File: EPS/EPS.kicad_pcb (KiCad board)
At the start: 2 copper layers, 219 parts, among them J1 CAN_BUS, J10 BOOT1, J11 ST_LINK, J12 USART, J9 BOOT0, Q1 Q_NMOS_GSD, Q10 Q_NMOS_GSD, Q11 Q_PMOS_GSD, Q12 Q_NMOS_DGS, Q13 PMOS_IN, Q14 Q_NMOS_GSD, Q15 PMOS_IN, Q16 PMOS_OUT1, Q17 PMOS_OUT2, Q18 NMOS_MCU, Q2 Q_NMOS_GSD, Q3 Q_NMOS_GSD, Q4 Q_NMOS_GSD, Q5 Q_PMOS_GSD, Q6 Q_NMOS_GSD, Q7 Q_NMOS_GSD, Q8 Q_PMOS_GSD, Q9 Q_PMOS_GSD, U1 MCP4728, U2 SN65HVD232, U3 SN65HVD232

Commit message: PCB updated
Added testpoints and updated PCB
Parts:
- removed 5V_1, 5V_2, Batt_V_1, Batt_V_2: Jst_Conn, Connectors_JST:JST_XH_B02B-XH-A_02x2.50mm_Straight
- removed J10: BOOT1, Pin_Headers:Pin_Header_Straight_1x03_Pitch2.54mm
- removed J9: BOOT0, Pin_Headers:Pin_Header_Straight_1x03_Pitch2.54mm
- removed Q18: NMOS_MCU, TO_SOT_Packages_SMD:SOT-23
- removed R5: 168k6, Resistors_SMD:R_0603
- removed R6: 30k1, Resistors_SMD:R_0603
- removed R62, R63, R64: R, Resistors_SMD:R_0603
- removed TPS1: TPS7A7002, Housings_SOIC:SOIC-8_3.9x4.9mm_Pitch1.27mm
- removed Temp_Connector1: JST_conn, Connectors_JST:JST_XH_B02B-XH-A_02x2.50mm_Straight
- added 3V6_1: Jst_Conn, Connectors_JST:JST_XH_B02B-XH-A_02x2.50mm_Straight, F.Cu at (145.5, 103.8)
- added 3V6_2: Jst_Conn, Connectors_JST:JST_XH_B02B-XH-A_02x2.50mm_Straight, F.Cu at (129.8, 103.5)
- added BOOT0: BOOT0, Pin_Headers:Pin_Header_Straight_1x03_Pitch2.54mm, F.Cu at (102.5, 103.8)
- added BOOT1: BOOT1, Pin_Headers:Pin_Header_Straight_1x03_Pitch2.54mm, F.Cu at (102.5, 94.8)
- added BU1: BU33SD5, Housings_SSOP:TSOP-5_1.65x3.05mm_Pitch0.95mm, F.Cu at (163.2, 106.2)
- added D4: LED, LEDs:LED_0603, F.Cu at (102.2, 87.8)
- added R65: 100, Resistors_SMD:R_0603, F.Cu at (106.2, 87.8)
- added RAW1: Jst_Conn, Connectors_JST:JST_XH_B02B-XH-A_02x2.50mm_Straight, F.Cu at (176.0, 91.8)
- added TP1: TEST, Measurement_Points:Measurement_Point_Round-SMD-Pad_Small, F.Cu at (121.9, 31.0)
- added TP10: TEST, Measurement_Points:Measurement_Point_Round-SMD-Pad_Small, F.Cu at (168.9, 31.2)
- added TP11: TEST, Measurement_Points:Measurement_Point_Round-SMD-Pad_Small, F.Cu at (125.0, 32.0)
- added TP12: TEST, Measurement_Points:Measurement_Point_Round-SMD-Pad_Small, F.Cu at (146.6, 32.3)
- added TP13: TEST, Measurement_Points:Measurement_Point_Round-SMD-Pad_Small, F.Cu at (122.9, 47.0)
- added TP14: TEST, Measurement_Points:Measurement_Point_Round-SMD-Pad_Small, F.Cu at (143.5, 46.5)
- added TP15: TEST, Measurement_Points:Measurement_Point_Round-SMD-Pad_Small, F.Cu at (166.9, 51.8)
- added TP16: TEST, Measurement_Points:Measurement_Point_Round-SMD-Pad_Small, F.Cu at (122.4, 53.8)
- added TP17: TEST, Measurement_Points:Measurement_Point_Round-SMD-Pad_Small, F.Cu at (128.0, 55.6)
- added TP18: TEST, Measurement_Points:Measurement_Point_Round-SMD-Pad_Small, F.Cu at (131.1, 58.2)
- added TP19: TEST, Measurement_Points:Measurement_Point_Round-SMD-Pad_Small, F.Cu at (148.1, 63.2)
- added TP2: TEST, Measurement_Points:Measurement_Point_Round-SMD-Pad_Small, F.Cu at (139.4, 31.0)
- added TP20: TEST, Measurement_Points:Measurement_Point_Round-SMD-Pad_Small, F.Cu at (148.1, 61.2)
- added TP21: TEST, Measurement_Points:Measurement_Point_Round-SMD-Pad_Small, F.Cu at (172.5, 55.9)
- added TP22: TEST, Measurement_Points:Measurement_Point_Round-SMD-Pad_Small, F.Cu at (176.0, 46.7)
- added TP23: TEST, Measurement_Points:Measurement_Point_Round-SMD-Pad_Small, F.Cu at (150.1, 55.1)
- added TP24: TEST, Measurement_Points:Measurement_Point_Round-SMD-Pad_Small, F.Cu at (156.7, 52.1)
- added TP25: TEST, Measurement_Points:Measurement_Point_Round-SMD-Pad_Small, F.Cu at (94.5, 72.1)
- added TP26: TEST, Measurement_Points:Measurement_Point_Round-SMD-Pad_Small, F.Cu at (94.5, 75.4)
- added TP27: TEST, Measurement_Points:Measurement_Point_Round-SMD-Pad_Small, F.Cu at (116.6, 22.1)
- added TP3: TEST, Measurement_Points:Measurement_Point_Round-SMD-Pad_Small, F.Cu at (157.5, 30.7)
- added TP4: TEST, Measurement_Points:Measurement_Point_Round-SMD-Pad_Small, F.Cu at (115.8, 28.7)
- added TP5: TEST, Measurement_Points:Measurement_Point_Round-SMD-Pad_Small, F.Cu at (133.6, 31.8)
- added TP6: TEST, Measurement_Points:Measurement_Point_Round-SMD-Pad_Small, F.Cu at (152.4, 31.5)
- added TP7: TEST, Measurement_Points:Measurement_Point_Round-SMD-Pad_Small, F.Cu at (167.1, 45.5)
- added TP8: TEST, Measurement_Points:Measurement_Point_Round-SMD-Pad_Small, F.Cu at (128.5, 44.2)
- added TP9: TEST, Measurement_Points:Measurement_Point_Round-SMD-Pad_Small, F.Cu at (149.9, 44.2)
- ABM3, C1, C10, C11, C12, C13, C14, C15, C16, C4, C5, C6, C7, C8, C9, L1, R3, R4, STM1, U2, U3: moved to B.Cu
- C2: value 0.1u -> 4.7u
- J1: footprint Housings_SOIC:SOIC-8_3.9x4.9mm_Pitch1.27mm -> Pin_Headers:Pin_Header_Straight_1x03_Pitch2.54mm
- Q5, Q8, Q9: value Q_PMOS_GSD -> PMOS_DIGITAL_LOAD?
- R_s4, R_s5, R_s6, R_s7, R_s8, R_s9: footprint Resistors_SMD:R_0603 -> Resistors_SMD:R_0805
- moved J1 221.4 mm to (190.6, 101.0)
- moved R4 218.7 mm to (184.4, 107.0), turned to 90 degrees
- moved R3 218.5 mm to (184.4, 101.2), turned to 90 degrees
- moved C15 201.6 mm to (172.4, 101.4), turned to 270 degrees
- moved C3 199.9 mm to (166.2, 106.0), turned to 270 degrees
- moved U2 196.1 mm to (177.4, 101.0)
- moved C54 195.1 mm to (147.2, 99.0), turned to 270 degrees
- moved C2 193.1 mm to (160.0, 106.0), turned to 270 degrees
- moved C9 193.0 mm to (152.5, 79.0), turned to 270 degrees
- moved U3 189.4 mm to (177.4, 106.8)
- moved C8 185.1 mm to (149.8, 65.5), turned to 90 degrees
- moved C6 183.8 mm to (146.8, 65.5), turned to 90 degrees
- moved C4 173.2 mm to (141.2, 65.5), turned to 90 degrees
- moved C1 172.5 mm to (131.2, 68.5), turned to 180 degrees
- moved STM1 167.1 mm to (144.0, 74.5)
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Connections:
- net /STM32_block/I_BATT2 renamed Net-(STM1-Pad25)
- BQ1 pad 5: GND -> /SW3
- BQ1 pad 6: GND -> /SW3
- BT2 pad 2: GND -> /SW3
- C57 pad 2: GND -> /SW3
- C58 pad 2: GND -> /SW3
- C59 pad 2: GND -> /SW3
- LM335A1 pad 1: /Battery_pack/BATT_TEMP -> /TEMP_BATT
- LM335A1 pad 2: GND -> /SW3
- MAX4 pad 3: /Connectors_diodes/Diode_enable -> /DIODE_EN
- MAX40200_1 pad 3: /Connectors_diodes/Diode_enable -> /DIODE_EN
- MAX5 pad 3: /Connectors_diodes/Diode_enable -> /DIODE_EN
- MAX6 pad 3: /Connectors_diodes/Diode_enable -> /DIODE_EN
- MAX7 pad 3: /Connectors_diodes/Diode_enable -> /DIODE_EN
- MAX8 pad 3: /Connectors_diodes/Diode_enable -> /DIODE_EN
- Q12 pad 2: /Battery_pack/BATT_HEATER -> /HEATER_EN
- Q12 pad 3: GND -> /SW3
- Q16 pad 1: Net-(Q16-Pad1) -> /SW2
- Q17 pad 1: Net-(Q16-Pad1) -> /SW2
- R48 pad 2: /Battery_pack/BATT_CELL2_VOLTAGE -> /BATT_V2
- R49 pad 2: /Battery_pack/BATT_CELL1_VOLTAGE -> /BATT_V1
- R50 pad 2: /Battery_pack/BATT_CELL2_VOLTAGE -> /BATT_V2
- R51 pad 2: /Battery_pack/BATT_CELL1_VOLTAGE -> /BATT_V1
- R56 pad 2: /Battery_pack/BATT_TEMP -> /TEMP_BATT
- R57 pad 1: /Battery_pack/BATT_HEATER -> /HEATER_EN
- R61 pad 1: /Battery_pack/BATT+ -> /SW2
- R61 pad 2: Net-(Q16-Pad1) -> /Battery_pack/BATT+
- RBF_control_pins1 pad 5: GND -> /SW3
- STM1 pad 16: Net-(STM1-Pad16) -> /TEMP_BATT
- STM1 pad 26: /STM32_block/TEMP_BATT1 -> /BATT_V1
- STM1 pad 27: /STM32_block/TEMP_BATT2 -> /BATT_V2
- STM1 pad 36: /3V6_BUS_SW2 -> /3V6_BUS_SW1
- STM1 pad 37: /STM32_block/BATT2_BUS_SW -> /INPUT_PWR_SW
- STM1 pad 39: /MAIN_PWR_SW -> Net-(STM1-Pad39)
- STM1 pad 51: Net-(STM1-Pad51) -> /DIODE_EN
- STM1 pad 52: Net-(STM1-Pad52) -> /HEATER_EN
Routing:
- net +3V3: track 8.05 -> 80.3 mm, vias 0 -> 4
- net GND: track 114.7 -> 160.6 mm, vias 14 -> 23
- net Net-(BT1-Pad2): track 0.00 -> 45.6 mm
- net /DIODE_EN: track 0.00 -> 40.2 mm, vias 0 -> 6
- net /Connectors_diodes/Diode_enable: track 38.0 -> 0.00 mm, vias 6 -> 0
- net /Input/Current_Limiters/DAC3: track 35.4 -> 0.00 mm, vias 2 -> 0
- net /SW3: track 0.00 -> 33.4 mm
- net /CAN_H: track 0.00 -> 31.3 mm
- net /SW2: track 0.00 -> 29.2 mm
- net /SW1: track 3.25 -> 32.0 mm, vias 0 -> 1
- net /Z_PV: track 21.9 -> 50.5 mm, vias 1 -> 2
- net Net-(OPAMP3-Pad3): track 33.7 -> 7.10 mm
- net /CAN_L: track 0.00 -> 25.7 mm, vias 0 -> 2
- net /X_PV: track 29.0 -> 45.7 mm
- net Net-(OPAMP1-Pad3): track 24.0 -> 7.73 mm
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- added copper zone on In1.Cu, net +3V3
- added copper zone on B.Cu, net GND
- added copper zone on In2.Cu, net GND
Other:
- board outline added: 100 x 100 mm
- copper layers 2 -> 4
- board text added: "+3V3"
- board text added: "CAN_H"
- board text added: "CAN_L"
- board text added: "GND"
- board text added: "NRST"
- board text added: "SWCLK"
- board text added: "SWDIO"
- board text added: "USART_RX"
- board text added: "USART_TX"

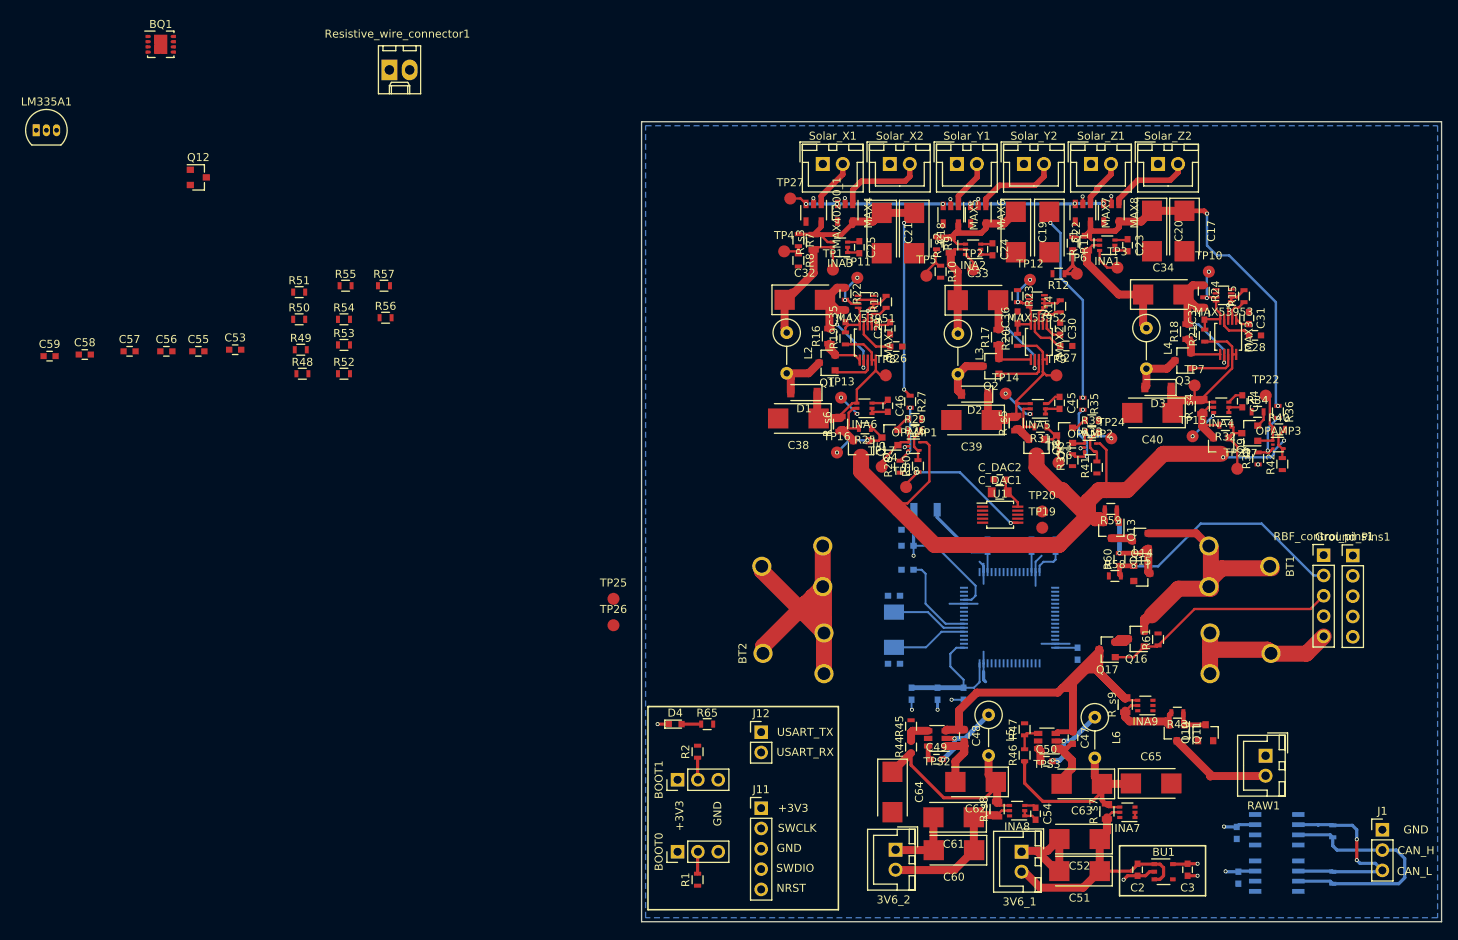
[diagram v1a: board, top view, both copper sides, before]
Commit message: Updated PCB
PCB requires mcu to be routed.
Changed to thermistor connector on pcb
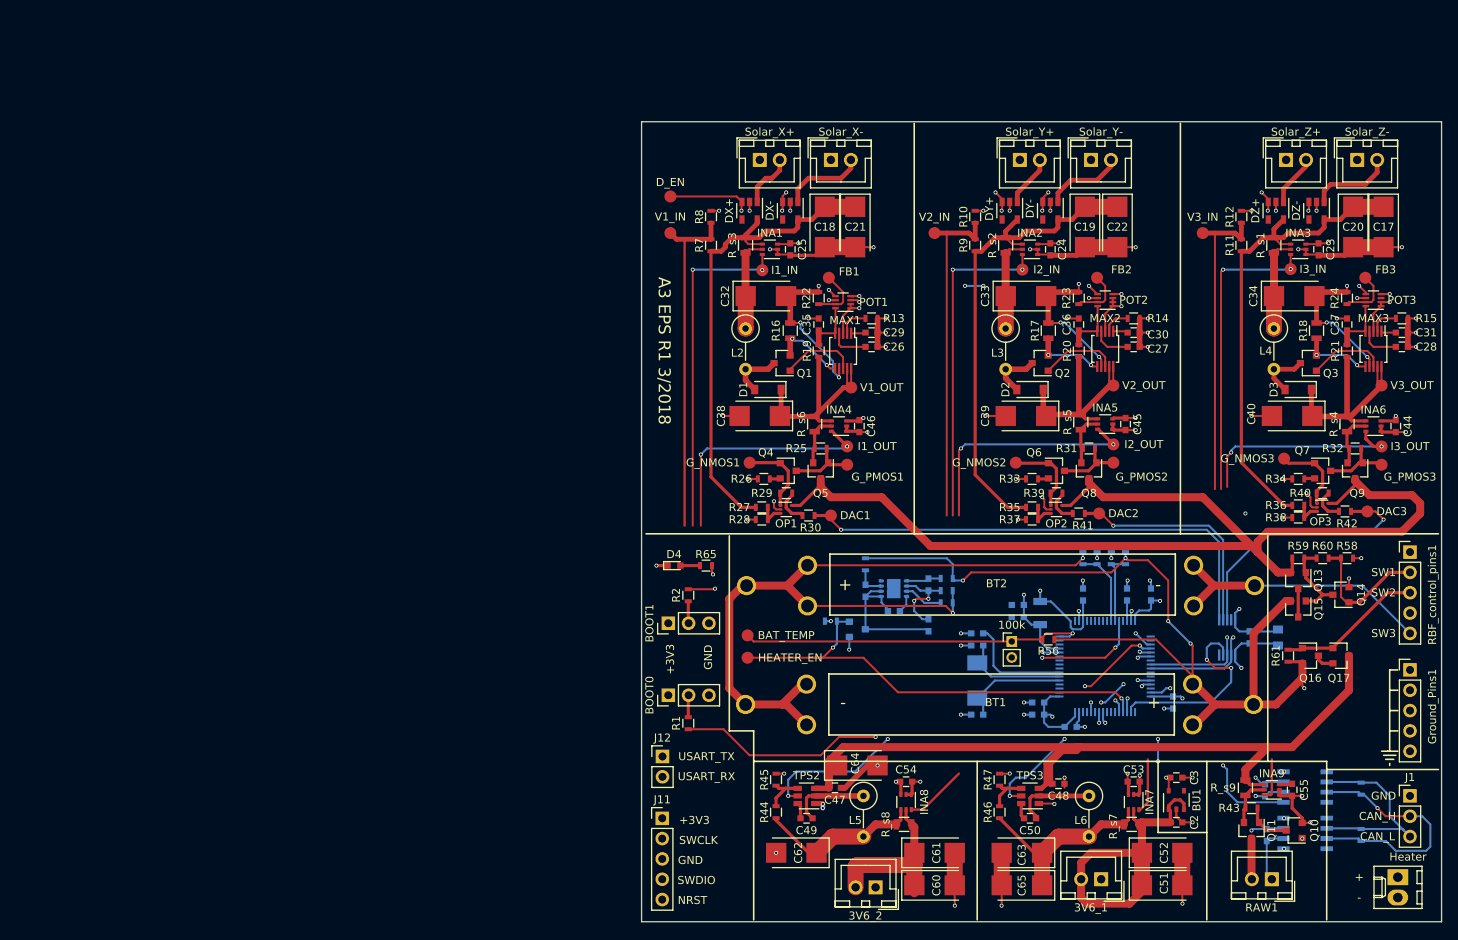
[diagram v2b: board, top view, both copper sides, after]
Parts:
- 100k: renamed from LM335A1; value D_Zener -> therm; footprint TO_SOT_Packages_THT:TO-92_Inline_Narrow_Oval -> Socket_Strips:Socket_Strip_Straight_1x02_Pitch2.00mm
- BQ1, C56, C57, C58, C59, C_DAC1, C_DAC2, Q12, R48, R49, R50, R51, R52, R53, R54, R55, R57, U1: moved to B.Cu
- moved Heater 161.5 mm to (192.5, 106.9), turned to 270 degrees
- moved C55 147.3 mm to (179.3, 96.0), turned to 270 degrees
- moved 100k 137.7 mm to (144.3, 77.5)
- moved C53 124.6 mm to (159.5, 95.0)
- moved BQ1 114.1 mm to (129.5, 70.9), turned to 180 degrees
- moved R50 107.5 mm to (158.5, 67.1), turned to 270 degrees
- moved C59 106.1 mm to (126.0, 71.1), turned to 270 degrees
- moved C58 106.1 mm to (129.5, 73.7), turned to 180 degrees
- moved C57 105.6 mm to (133.9, 75.4), turned to 270 degrees
- moved R48 103.7 mm to (156.7, 67.1), turned to 270 degrees
- moved R51 103.5 mm to (153.2, 67.1), turned to 270 degrees
- moved R49 102.9 mm to (154.9, 67.1), turned to 270 degrees
- moved Q12 99.9 mm to (125.0, 75.9)
- moved C56 99.6 mm to (133.9, 70.4), turned to 270 degrees
- moved R56 92.1 mm to (148.8, 77.2), turned to 180 degrees
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- renumbered TP25 to BAT_TEMP, TP18 to DAC1, TP19 to DAC2, TP20 to DAC3, MAX40200_1 to DX+, MAX4 to DX-, MAX5 to DY+, MAX6 to DY-, MAX7 to DZ+, MAX8 to DZ-, TP27 to D_EN, TP11 to FB1, TP12 to FB2, TP10 to FB3, TP17 to G_NMOS1, TP24 to G_NMOS2, TP22 to G_NMOS3, TP16 to G_PMOS1, TP23 to G_PMOS2, TP21 to G_PMOS3, TP26 to HEATER_EN, Resistive_wire_connector1 to Heater, TP1 to I1_IN, TP13 to I1_OUT, TP2 to I2_IN, TP14 to I2_OUT, TP3 to I3_IN, TP15 to I3_OUT, INA3 to INA1, INA1 to INA3, INA6 to INA4, INA4 to INA6, OPAMP1 to OP1, OPAMP2 to OP2, OPAMP3 to OP3, MAX53951 to POT1, MAX53952 to POT2, MAX53953 to POT3, Solar_X1 to Solar_X+, Solar_X2 to Solar_X-, Solar_Y1 to Solar_Y+, Solar_Y2 to Solar_Y-, Solar_Z1 to Solar_Z+, Solar_Z2 to Solar_Z-, TP4 to V1_IN, TP8 to V1_OUT, TP5 to V2_IN, TP9 to V2_OUT, TP6 to V3_IN, TP7 to V3_OUT
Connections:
- 100k pad 2: /SW3 -> +3V3
- BU1 pad 4: Net-(BU1-Pad4) -> (no net)
- C64 pad 1: /Bus_regulation/3V6_rail/3V6_BUS1 -> /Bus_regulation/VIN
- DX+ pad 4: Net-(MAX40200_1-Pad4) -> (no net)
- DX- pad 4: Net-(MAX4-Pad4) -> (no net)
- DY+ pad 4: Net-(MAX5-Pad4) -> (no net)
- DY- pad 4: Net-(MAX6-Pad4) -> (no net)
- DZ+ pad 4: Net-(MAX7-Pad4) -> (no net)
- DZ- pad 4: Net-(MAX8-Pad4) -> (no net)
- POT3 pad 3: Net-(MAX53953-Pad3) -> (no net)
- RBF_control_pins1 pad 1: /Connectors_diodes/RBF_POWER -> (no net)
- RBF_control_pins1 pad 4: /Connectors_diodes/DSW_2 -> (no net)
- STM1 pad 2: Net-(STM1-Pad2) -> (no net)
- STM1 pad 25: Net-(STM1-Pad25) -> (no net)
- STM1 pad 29: Net-(STM1-Pad29) -> (no net)
- STM1 pad 3: Net-(STM1-Pad3) -> (no net)
- STM1 pad 33: Net-(STM1-Pad33) -> (no net)
- STM1 pad 34: Net-(STM1-Pad34) -> (no net)
- STM1 pad 39: Net-(STM1-Pad39) -> (no net)
- STM1 pad 4: Net-(STM1-Pad4) -> (no net)
- STM1 pad 54: Net-(STM1-Pad54) -> (no net)
- STM1 pad 55: Net-(STM1-Pad55) -> (no net)
- STM1 pad 56: Net-(STM1-Pad56) -> (no net)
- STM1 pad 59: Net-(STM1-Pad59) -> (no net)
- STM1 pad 61: Net-(STM1-Pad61) -> (no net)
- STM1 pad 62: Net-(STM1-Pad62) -> (no net)
- U1 pad 5: Net-(U1-Pad5) -> (no net)
- U1 pad 9: Net-(U1-Pad9) -> (no net)
- U2 pad 5: Net-(U2-Pad5) -> (no net)
- U2 pad 8: Net-(U2-Pad8) -> (no net)
- U3 pad 5: Net-(U3-Pad5) -> (no net)
- U3 pad 8: Net-(U3-Pad8) -> (no net)
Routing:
- net /SCL: track 0.00 -> 129.7 mm, vias 0 -> 7
- net /SDA: track 0.00 -> 126.7 mm, vias 0 -> 4
- net /DIODE_EN: track 40.2 -> 164.0 mm, vias 6 -> 11
- net /Battery_pack/BATT+: track 33.6 -> 151.4 mm, vias 0 -> 5
- net GND: track 160.6 -> 275.3 mm, vias 23 -> 91
- net Net-(Q12-Pad1): track 0.00 -> 93.3 mm, vias 0 -> 1
- net Net-(R2-Pad1): track 0.00 -> 68.7 mm, vias 0 -> 3
- net Net-(R65-Pad2): track 0.00 -> 62.2 mm, vias 0 -> 2
- net /HEATER_EN: track 0.00 -> 58.8 mm, vias 0 -> 2
- net /3V6_BUS_SW1: track 0.00 -> 56.7 mm, vias 0 -> 4
- net Net-(R1-Pad2): track 0.00 -> 56.3 mm, vias 0 -> 2
- net Net-(BT1-Pad2): track 45.6 -> 98.8 mm, vias 0 -> 2
- net /Bus_regulation/VIN: track 56.2 -> 101.1 mm
- net /Input/Current_Limiters/DAC1: track 17.7 -> 62.0 mm, vias 2 -> 1
- net /TEMP_BATT: track 0.00 -> 43.2 mm, vias 0 -> 1
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- removed copper zone on B.Cu, net GND
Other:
- board text added: "+"
- board text added: "-"
- board text added: "A3 EPS R1 3/2018"
- board text added: "SW1"
- board text added: "SW2"
- board text added: "SW3"
